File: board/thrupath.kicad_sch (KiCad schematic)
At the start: 114 parts, among them J6 BEL_FUSE_0826-1G1T-23-F, J7 BEL_FUSE_0826-1G1T-23-F, U4 XC7S15-1FTGB196C, U5 KSZ9031RN, U6 KSZ9031RN, U7 OSC, U8 OSC

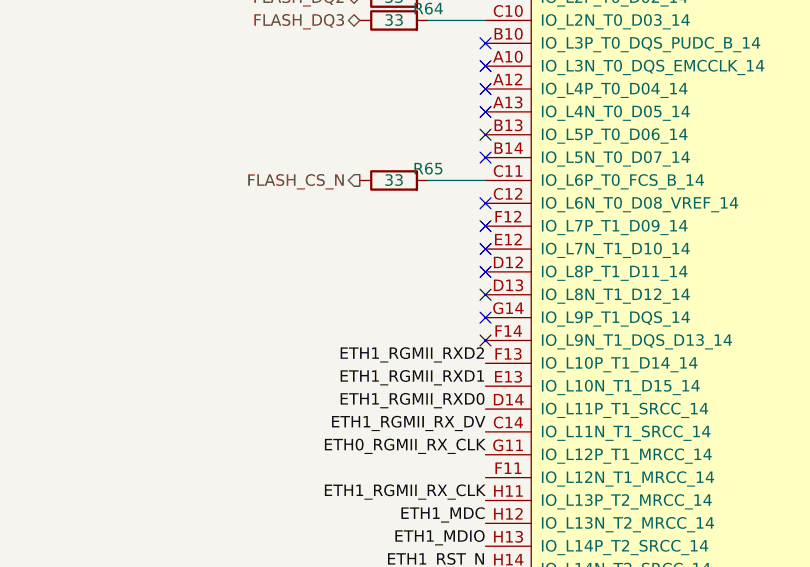
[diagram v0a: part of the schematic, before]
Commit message: Continued initial schematic capture
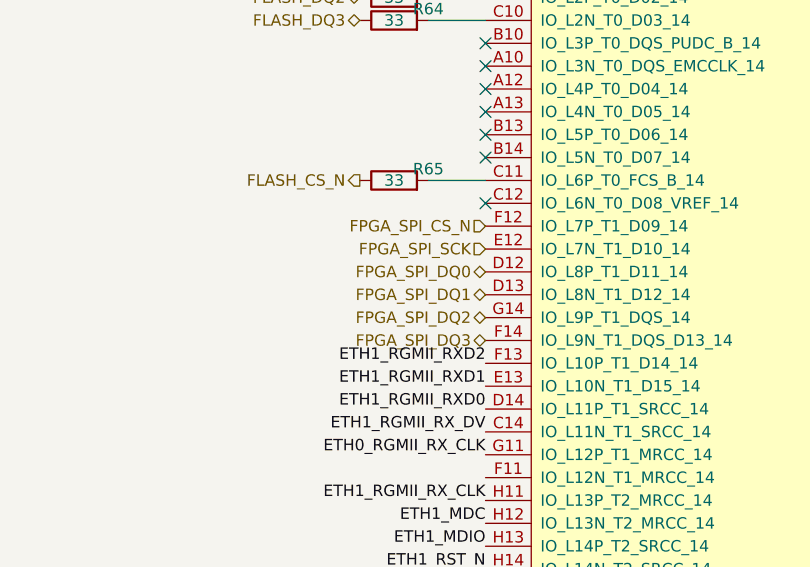
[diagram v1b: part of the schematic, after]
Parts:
- R61, R62, R63, R64, R65: footprint (none) -> azonenberg_pcb:EIA_0402_RES_NOSILK
- U4: footprint (none) -> azonenberg_pcb:BGA_196_15x15_FULLARRAY_1MM_FTGB196
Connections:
- net FPGA_SPI_DQ0: now reaches U4.D12 (IO_L8P_T1_D11_14)
- net FPGA_SPI_DQ1: now reaches U4.D13 (IO_L8N_T1_D12_14)
- net FPGA_SPI_SCK: now reaches U4.E12 (IO_L7N_T1_D10_14)
- net FPGA_SPI_CS_N: now reaches U4.F12 (IO_L7P_T1_D09_14)
- net FPGA_SPI_DQ3: now reaches U4.F14 (IO_L9N_T1_DQS_D13_14)
- net FPGA_SPI_DQ2: now reaches U4.G14 (IO_L9P_T1_DQS_14)
- no-connect marks 19 -> 13
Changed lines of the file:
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@@
   (no_connect (at 364.49 35.56))
   (no_connect (at 364.49 50.8))
-  (no_connect (at 364.49 66.04))
   (no_connect (at 364.49 38.1))
   (no_connect (at 364.49 40.64))
   (no_connect (at 364.49 43.18))
   (no_connect (at 364.49 45.72))
-  (no_connect (at 364.49 53.34))
-  (no_connect (at 364.49 55.88))
-  (no_connect (at 364.49 58.42))
-  (no_connect (at 364.49 60.96))
-  (no_connect (at 364.49 63.5))
   (no_connect (at 143.51 76.2))
   (no_connect (at 86.36 68.58))
@@
     (effects (font (size 1.27 1.27)) (justify right))
   )
+  (hierarchical_label "FPGA_SPI_CS_N" (shape input) (at 364.49 53.34 180)
+    (effects (font (size 1.27 1.27)) (justify right))
+  )
   (hierarchical_label "FLASH_DQ2" (shape bidirectional) (at 350.52 27.94 180)
     (effects (font (size 1.27 1.27)) (justify right))
@@
     (effects (font (size 1.27 1.27)) (justify right))
   )
+  (hierarchical_label "FPGA_SPI_DQ2" (shape bidirectional) (at 364.49 63.5 180)
+    (effects (font (size 1.27 1.27)) (justify right))
+  )
+  (hierarchical_label "FPGA_SPI_DQ3" (shape bidirectional) (at 364.49 66.04 180)
+    (effects (font (size 1.27 1.27)) (justify right))
+  )
+  (hierarchical_label "FPGA_SPI_SCK" (shape input) (at 364.49 55.88 180)
+    (effects (font (size 1.27 1.27)) (justify right))
+  )
   (hierarchical_label "FLASH_CS_N" (shape output) (at 350.52 48.26 180)
     (effects (font (size 1.27 1.27)) (justify right))
@@
   )
   (hierarchical_label "FLASH_DQ3" (shape bidirectional) (at 350.52 30.48 180)
+    (effects (font (size 1.27 1.27)) (justify right))
+  )
+  (hierarchical_label "FPGA_SPI_DQ1" (shape bidirectional) (at 364.49 60.96 180)
+    (effects (font (size 1.27 1.27)) (justify right))
+  )
+  (hierarchical_label "FPGA_SPI_DQ0" (shape bidirectional) (at 364.49 58.42 180)
     (effects (font (size 1.27 1.27)) (justify right))
   )
@@
     (property "Reference" "R64" (id 0) (at 358.14 29.21 90))
     (property "Value" "33" (id 1) (at 354.33 30.48 90))
-    (property "Footprint" "" (id 2) (at 354.33 32.258 90)
+    (property "Footprint" "azonenberg_pcb:EIA_0402_RES_NOSILK" (id 2) (at 354.33 32.258 90)
       (effects (font (size 1.27 1.27)) hide)
     )
@@
     (property "Reference" "R61" (id 0) (at 358.14 21.59 90))
     (property "Value" "33" (id 1) (at 354.33 22.86 90))
-    (property "Footprint" "" (id 2) (at 354.33 24.638 90)
+    (property "Footprint" "azonenberg_pcb:EIA_0402_RES_NOSILK" (id 2) (at 354.33 24.638 90)
       (effects (font (size 1.27 1.27)) hide)
     )
@@
     (property "Reference" "R63" (id 0) (at 358.14 26.67 90))
     (property "Value" "33" (id 1) (at 354.33 27.94 90))
-    (property "Footprint" "" (id 2) (at 354.33 29.718 90)
+    (property "Footprint" "azonenberg_pcb:EIA_0402_RES_NOSILK" (id 2) (at 354.33 29.718 90)
       (effects (font (size 1.27 1.27)) hide)
     )
@@
     (property "Reference" "R65" (id 0) (at 358.14 46.99 90))
     (property "Value" "33" (id 1) (at 354.33 48.26 90))
-    (property "Footprint" "" (id 2) (at 354.33 50.038 90)
+    (property "Footprint" "azonenberg_pcb:EIA_0402_RES_NOSILK" (id 2) (at 354.33 50.038 90)
       (effects (font (size 1.27 1.27)) hide)
     )
@@
     (property "Reference" "R62" (id 0) (at 358.14 24.13 90))
     (property "Value" "33" (id 1) (at 354.33 25.4 90))
-    (property "Footprint" "" (id 2) (at 354.33 27.178 90)
+    (property "Footprint" "azonenberg_pcb:EIA_0402_RES_NOSILK" (id 2) (at 354.33 27.178 90)
       (effects (font (size 1.27 1.27)) hide)
     )
@@
     (property "Reference" "U4" (id 0) (at 379.73 15.24 0))
     (property "Value" "XC7S15-1FTGB196C" (id 1) (at 379.73 18.0151 0))
-    (property "Footprint" "" (id 2) (at 369.57 146.05 0)
-      (effects (font (size 1.27 1.27)) hide)
-    )
+    (property "Footprint" "azonenberg_pcb:BGA_196_15x15_FULLARRAY_1MM_FTGB196" (id 2) (at 369.57 146.05 0)
+      (effects (font (size 1.27 1.27)) hide)
+    )

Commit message: Finished initial schematic, ready for signoff review
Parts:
- U7, U8: value OSC -> ECS-2016MVQ-250-CN-TR; footprint (none) -> azonenberg_pcb:OSCILLATOR_2.0x1.6
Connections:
- net FPGA_IRQ: now reaches U4.A10 (IO_L3N_T0_DQS_EMCCLK_14)
- net A3V3 renamed ETH0_A3V3
- net ETH0_A3V3: no longer C60.1, C64.1, C65.1, C67.1, FB4.2, U6.1 (AVDDH), U6.12 (AVDDH), U6.47 (NC/AVDDH)
- new net ETH1_A3V3: C60.1, C64.1, C65.1, C67.1, FB4.2, U6.1 (AVDDH), U6.12 (AVDDH), U6.47 (NC/AVDDH)
- no-connect marks 13 -> 14
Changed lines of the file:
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@@
   (no_connect (at 143.51 176.53))
   (no_connect (at 143.51 87.63))
+  (no_connect (at 364.49 20.32))
+  (no_connect (at 364.49 81.28))
   (no_connect (at 86.36 157.48))
-  (no_connect (at 364.49 33.02))
-  (no_connect (at 364.49 35.56))
-  (no_connect (at 364.49 50.8))
   (no_connect (at 364.49 38.1))
   (no_connect (at 364.49 40.64))
   (no_connect (at 364.49 43.18))
   (no_connect (at 364.49 45.72))
+  (no_connect (at 364.49 33.02))
+  (no_connect (at 364.49 50.8))
   (no_connect (at 143.51 76.2))
   (no_connect (at 86.36 68.58))
@@
     (effects (font (size 1.27 1.27)) (justify left bottom))
   )
-  (label "A3V3" (at 82.55 207.01 0)
+  (label "ETH0_A3V3" (at 82.55 207.01 0)
     (effects (font (size 1.27 1.27)) (justify left bottom))
   )
@@
     (effects (font (size 1.27 1.27)) (justify right bottom))
   )
-  (label "A3V3" (at 262.89 207.01 0)
+  (label "ETH1_A3V3" (at 262.89 207.01 0)
     (effects (font (size 1.27 1.27)) (justify left bottom))
   )
@@
     (effects (font (size 1.27 1.27)) (justify right bottom))
   )
-  (label "A3V3" (at 73.66 26.67 180)
+  (label "ETH0_A3V3" (at 73.66 26.67 180)
     (effects (font (size 1.27 1.27)) (justify right bottom))
   )
@@
     (effects (font (size 1.27 1.27)) (justify left bottom))
   )
-  (label "A3V3" (at 73.66 115.57 180)
+  (label "ETH1_A3V3" (at 73.66 115.57 180)
     (effects (font (size 1.27 1.27)) (justify right bottom))
   )
@@
   )
   (hierarchical_label "FPGA_SPI_SCK" (shape input) (at 364.49 55.88 180)
+    (effects (font (size 1.27 1.27)) (justify right))
+  )
+  (hierarchical_label "FPGA_IRQ" (shape output) (at 364.49 35.56 180)
     (effects (font (size 1.27 1.27)) (justify right))
   )
@@
       (effects (font (size 1.524 1.524)))
     )
-    (property "Value" "OSC" (id 1) (at 128.905 231.6226 0)
+    (property "Value" "ECS-2016MVQ-250-CN-TR" (id 1) (at 128.905 231.6226 0)
       (effects (font (size 1.524 1.524)))
     )
-    (property "Footprint" "" (id 2) (at 129.54 236.22 0)
+    (property "Footprint" "azonenberg_pcb:OSCILLATOR_2.0x1.6" (id 2) (at 129.54 236.22 0)
       (effects (font (size 1.524 1.524)) hide)
     )
@@
       (effects (font (size 1.524 1.524)))
     )
-    (property "Value" "OSC" (id 1) (at 309.245 231.6226 0)
+    (property "Value" "ECS-2016MVQ-250-CN-TR" (id 1) (at 309.245 231.6226 0)
       (effects (font (size 1.524 1.524)))
     )
-    (property "Footprint" "" (id 2) (at 309.88 236.22 0)
+    (property "Footprint" "azonenberg_pcb:OSCILLATOR_2.0x1.6" (id 2) (at 309.88 236.22 0)
       (effects (font (size 1.524 1.524)) hide)
     )
